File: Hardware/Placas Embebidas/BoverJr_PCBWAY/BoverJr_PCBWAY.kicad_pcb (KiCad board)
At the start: 2 copper layers, 100 x 100 mm, 38 parts, among them J1 Encoder Derecho, J10 7.4v, J2 Encoder Izquierdo, J3 Programador, J4 Distancia_Der, J5 Distancia_Izq, J8 Distancia_Frontal, SW1 SW_SPDT, U1 ESP32-WROOM-32E, U2 MPU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

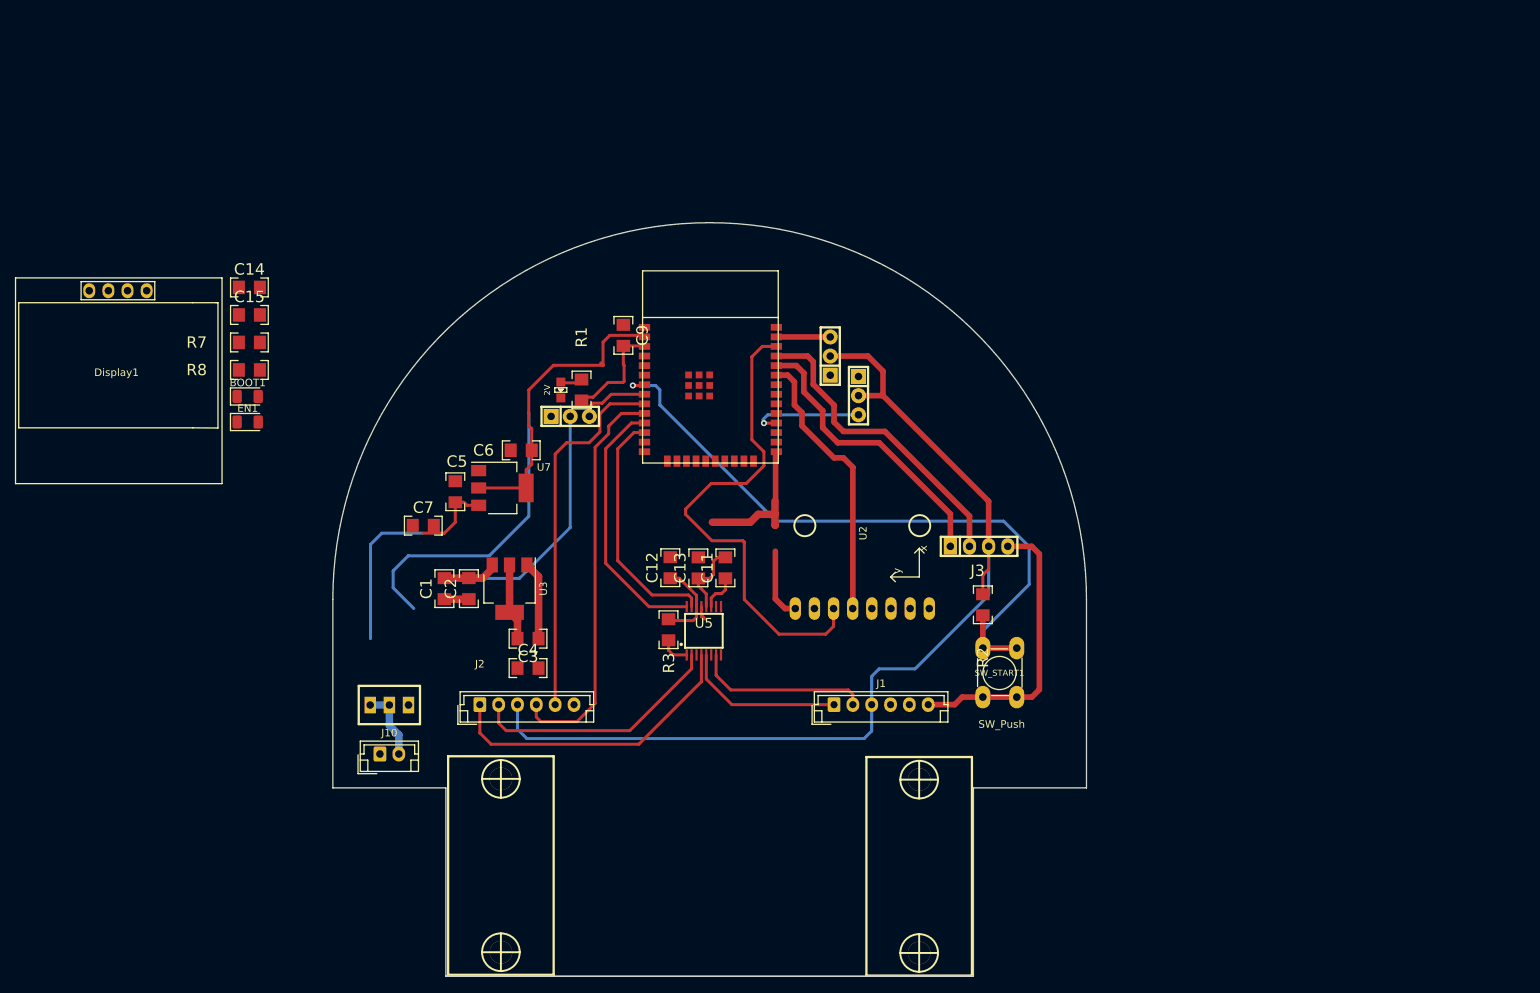
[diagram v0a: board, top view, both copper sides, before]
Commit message: Placa falta verificar sch nuevamente , el 3d y los empaquetados de componentes quevamos a usar
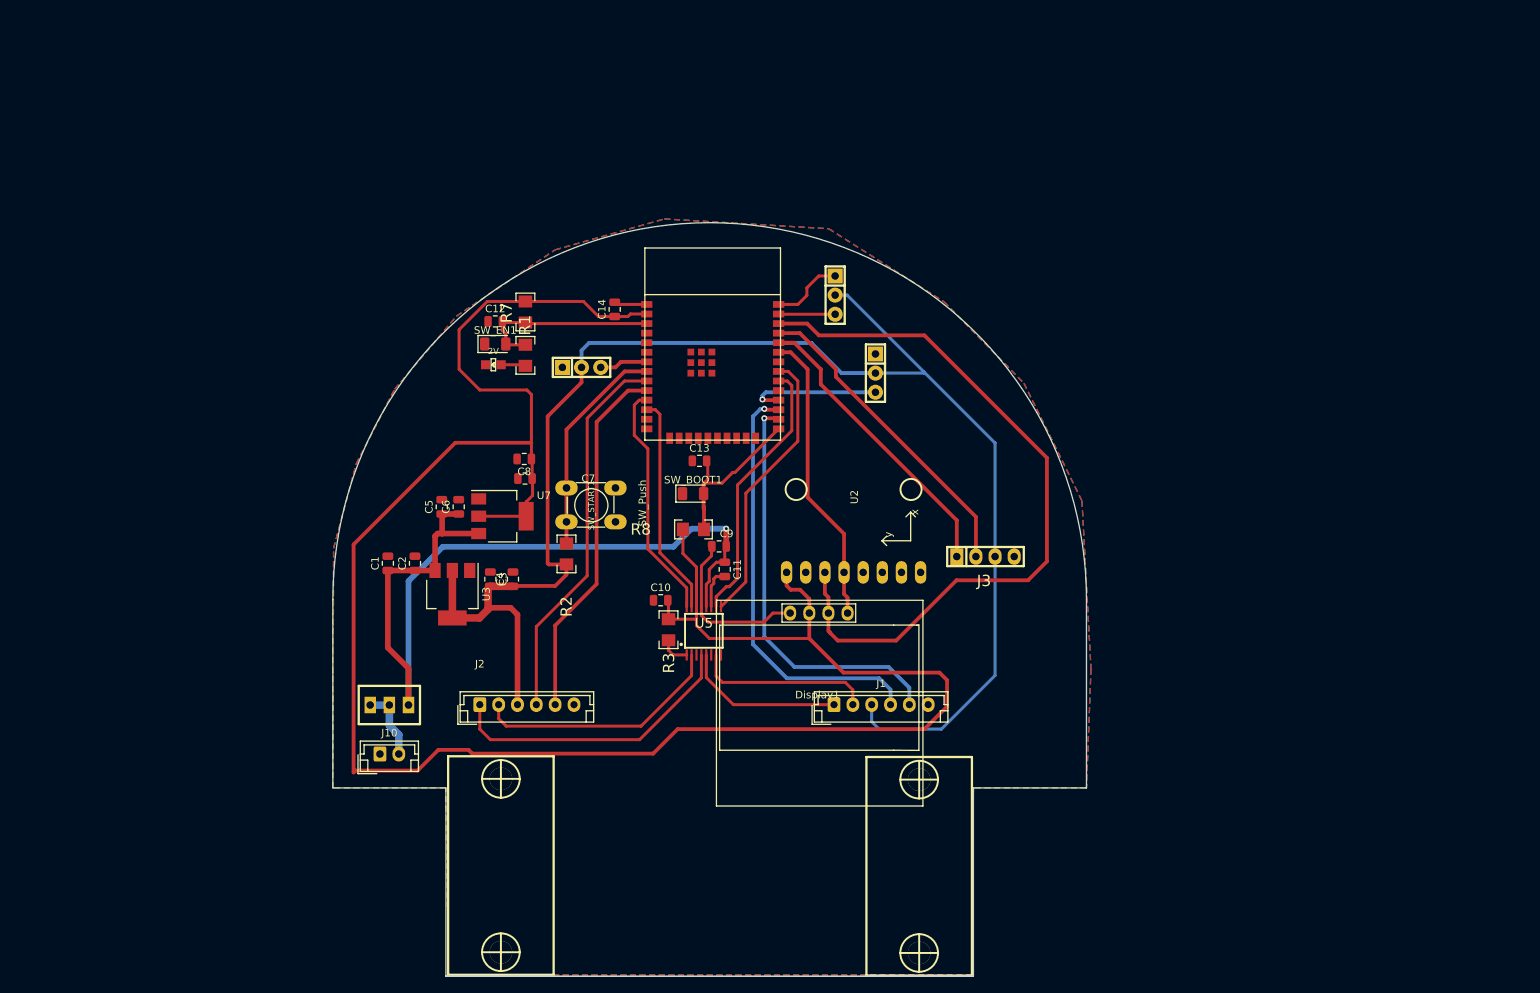
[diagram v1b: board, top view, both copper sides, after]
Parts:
- added C14: 100nF, Capacitor_SMD:C_0805_2012Metric, F.Cu at (137.4, 41.3)
- C1, C11, C2: footprint EESTN5:C_1206 -> Capacitor_SMD:C_0805_2012Metric
- C10: renamed from C12; footprint EESTN5:C_1206 -> Capacitor_SMD:C_0805_2012Metric
- C12: renamed from C14; value 1n -> 1nf; footprint EESTN5:C_1206 -> Capacitor_SMD:C_0805_2012Metric
- C13: renamed from C15; value 1n -> 1nf; footprint EESTN5:C_1206 -> Capacitor_SMD:C_0805_2012Metric
- C3, C7: value 10uF -> 100nF; footprint EESTN5:C_1206 -> Capacitor_SMD:C_0805_2012Metric
- C4: value 100nF -> 10uF; footprint EESTN5:C_1206 -> Capacitor_SMD:C_0805_2012Metric
- C5: renamed from C9; footprint EESTN5:C_1206 -> Capacitor_SMD:C_0805_2012Metric
- C6: renamed from C5; footprint EESTN5:C_1206 -> Capacitor_SMD:C_0805_2012Metric
- C8: renamed from C6; value 100nF -> 10uF; footprint EESTN5:C_1206 -> Capacitor_SMD:C_0805_2012Metric
- C9: renamed from C13; footprint EESTN5:C_1206 -> Capacitor_SMD:C_0805_2012Metric
- moved Display1 102.4 mm to (164.3, 92.2)
- moved C13 62.8 mm to (148.7, 61.4)
- moved R8 62.6 mm to (147.8, 70.5)
- moved SW_BOOT1 60.5 mm to (147.8, 65.8)
- moved SW_START1 60.0 mm to (137.5, 65.0), turned to -90 degrees
- moved R2 55.7 mm to (131.0, 73.8)
- moved R7 36.8 mm to (125.5, 41.6), turned to -90 degrees
- moved SW_EN1 34.4 mm to (121.5, 45.9)
- moved C5 33.1 mm to (114.5, 67.5), turned to 90 degrees
- moved C12 32.9 mm to (121.5, 42.9)
- moved C7 14.9 mm to (125.5, 63.8), turned to 180 degrees
- moved C4 12.0 mm to (123.9, 77.1), turned to 90 degrees
- moved LED_ESP32 9.56 mm to (121.3, 48.6), turned to 180 degrees
- moved C3 9.34 mm to (120.9, 77.1), turned to -90 degrees
- moved R1 8.76 mm to (125.5, 47.4)
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- renumbered BOOT1 to SW_BOOT1, EN1 to SW_EN1
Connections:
- C1 pad 1: +BATT -> VCC
- C2 pad 1: +BATT -> VCC
- C3 pad 1: +5V -> GND
- C3 pad 2: GND -> +5V
- C4 pad 1: GND -> +5V
- C4 pad 2: +5V -> GND
- C5 pad 1: +BATT -> VCC
- C6 pad 1: +BATT -> VCC
- R7 pad 2: +3V3 -> +3.3V
- R8 pad 2: +3V3 -> +3.3V
- U1 pad 10: /OUT_M2_DA -> /OUT_M2_DB
- U1 pad 7: /START -> /IR_DER
- U1 pad 8: /IR_DER -> /START
- U1 pad 9: /OUT_M2_DB -> /OUT_M2_DA
- U3 pad 3: +BATT -> VCC
- U7 pad 3: +BATT -> VCC
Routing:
- net +3.3V: track 102.1 -> 279.8 mm
- net VCC: track 9.97 -> 114.4 mm, vias 0 -> 1
- net /START: track 89.1 -> 28.9 mm, vias 1 -> 0
- net /OUT_M1_DA: track 0.00 -> 56.8 mm, vias 0 -> 1
- net /OUT_M1_DB: track 0.00 -> 55.3 mm, vias 0 -> 1
- net +BATT: track 47.8 -> 9.56 mm
- net /M1_IN1: track 0.00 -> 37.2 mm
- net /M1_IN2: track 0.00 -> 35.7 mm
- net /SCL: track 65.9 -> 98.6 mm
- net +5V: track 176.5 -> 205.6 mm
- net GND: track 53.8 -> 36.9 mm
- net /EN: track 14.2 -> 25.1 mm
- net /BOOT: track 18.6 -> 22.6 mm
- net /M2_IN1: track 34.9 -> 31.6 mm
- net /M2_IN2: track 32.3 -> 29.3 mm
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- added copper zone on B.Cu, net GND
- added copper zone on F.Cu, net GND

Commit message: hice cambiecitos
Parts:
- moved J3 6.92 mm to (188.0, 67.3), turned to 90 degrees
- moved J4 0.80 mm to (171.7, 49.0), turned to 0 degrees
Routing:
- net +5V: track 205.6 -> 212.4 mm
- net /IR_IZQ: track 17.9 -> 22.8 mm
- net /RX: track 39.4 -> 43.2 mm
- net GND: track 36.9 -> 38.3 mm
- net /OUT_M2_DA: track 50.7 -> 51.9 mm
- net /M1_IN1: track 37.2 -> 38.1 mm
- net /OUT_M2_DB: track 48.2 -> 49.0 mm
- net /OUT_A_MOTOR2: track 39.7 -> 39.0 mm

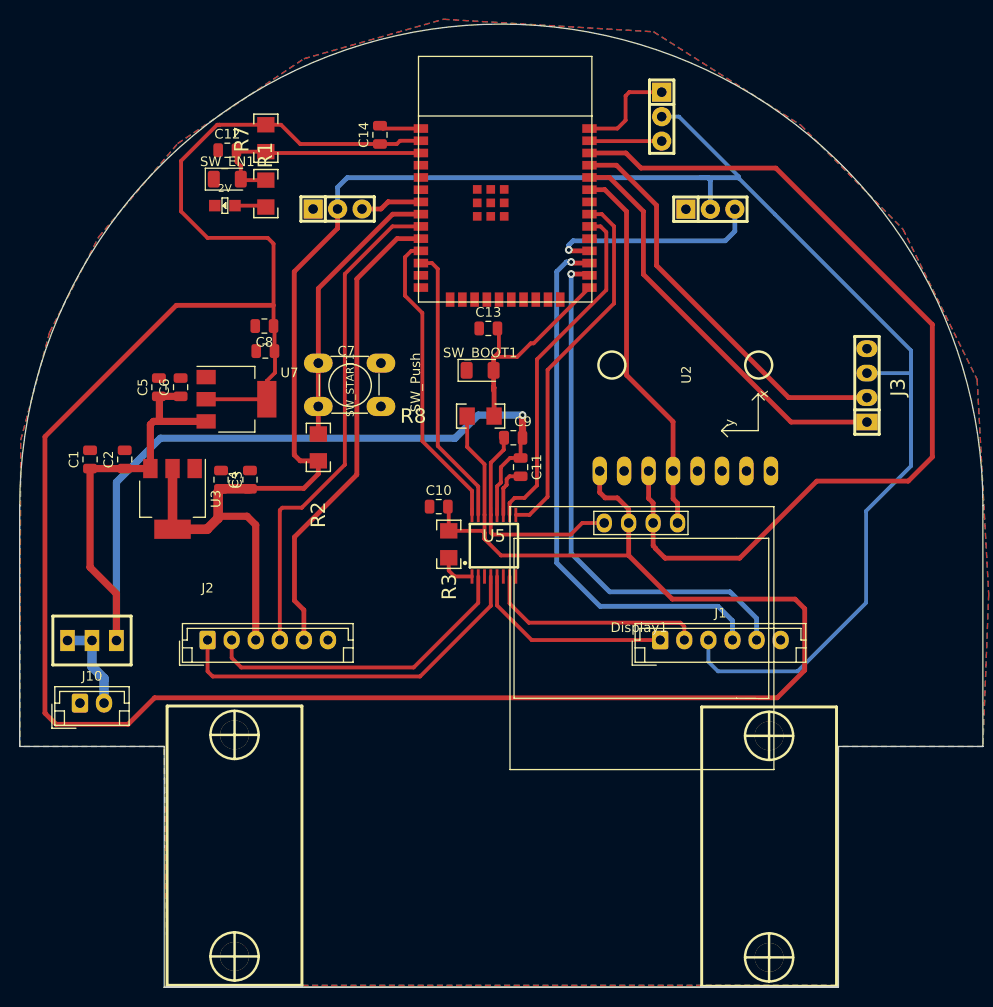
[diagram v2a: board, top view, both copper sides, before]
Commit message: FALTA VER EL TEMA DE LOS MOTORES SI SE PUEDE ACHICAR, ACOMODAR SERIGRAFIA Y AÑADIR LOGOS Y VERIFICAR X 3D , Y VER SI PODEMOS PONER JST
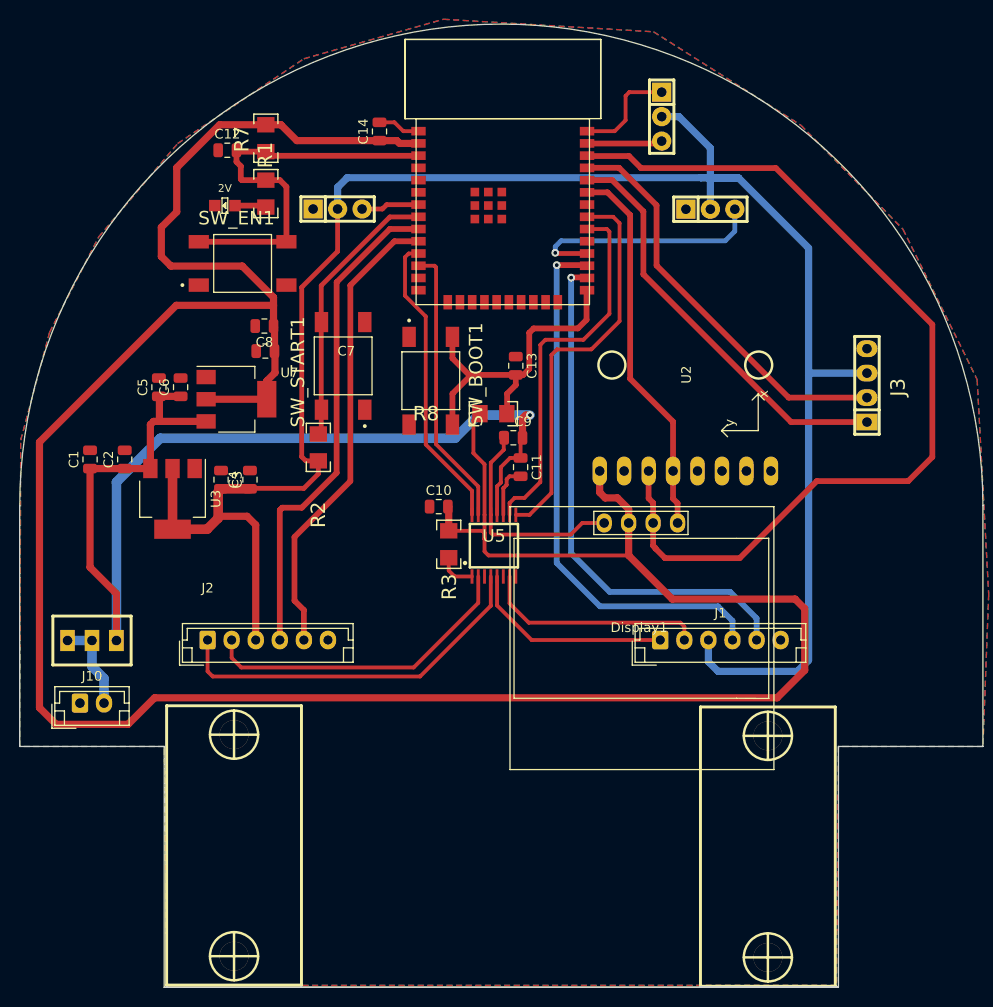
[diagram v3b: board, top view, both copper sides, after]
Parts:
- SW_BOOT1: value SW_Push -> BOOT; footprint Diode_SMD:D_1206_3216Metric -> EESTN5:SW_TL3301FF160QG
- SW_EN1: value SW_Push -> EN; footprint Diode_SMD:D_1206_3216Metric -> EESTN5:SW_TL3301FF160QG
- SW_START1: value SW_Push -> START; footprint EESTN5:PUSH_SWITCH_THT -> EESTN5:SW_TL3301FF160QG
- moved SW_EN1 8.89 mm to (123.1, 54.6)
- moved SW_BOOT1 5.24 mm to (142.7, 66.8), turned to -90 degrees
- moved C13 4.81 mm to (151.5, 65.3), turned to -90 degrees
- moved SW_START1 3.94 mm to (133.6, 65.3), turned to 90 degrees
- moved R8 1.35 mm to (149.2, 70.2)
- moved U1 0.37 mm to (150.2, 49.2)
- moved C14 0.35 mm to (137.3, 41.0)
- moved H2 0.12 mm to (177.7, 115.2)
- moved H1 0.06 mm to (122.2, 115.1)
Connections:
- SW_BOOT1 pad 2: /BOOT -> GND
- SW_EN1 pad 2: /EN -> GND
- SW_START1 pad 2: /START -> GND
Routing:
- net /EN: track 25.1 -> 42.2 mm
- net /BOOT: track 22.6 -> 34.9 mm
- net +5V: track 212.4 -> 206.3 mm
- net +3.3V: track 280.3 -> 283.6 mm
- net /M1_IN1: track 38.1 -> 41.3 mm
- net /M1_IN2: track 36.1 -> 39.0 mm
- net /IR_IZQ: track 22.8 -> 25.6 mm
- net VCC: track 114.4 -> 115.8 mm
- net /OUT_M1_DB: track 55.3 -> 54.6 mm
